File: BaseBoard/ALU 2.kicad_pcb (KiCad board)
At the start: 2 copper layers, 26 parts, among them J1 CONN_01X04, J2 CONN_01X04, J3 CONN_01X03, J4 CONN_01X08, J5 CONN_01X01, J6 CONN_01X04, J7 USB_OTG, U1 74LS138, U10 74LS244, U11 74LS08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

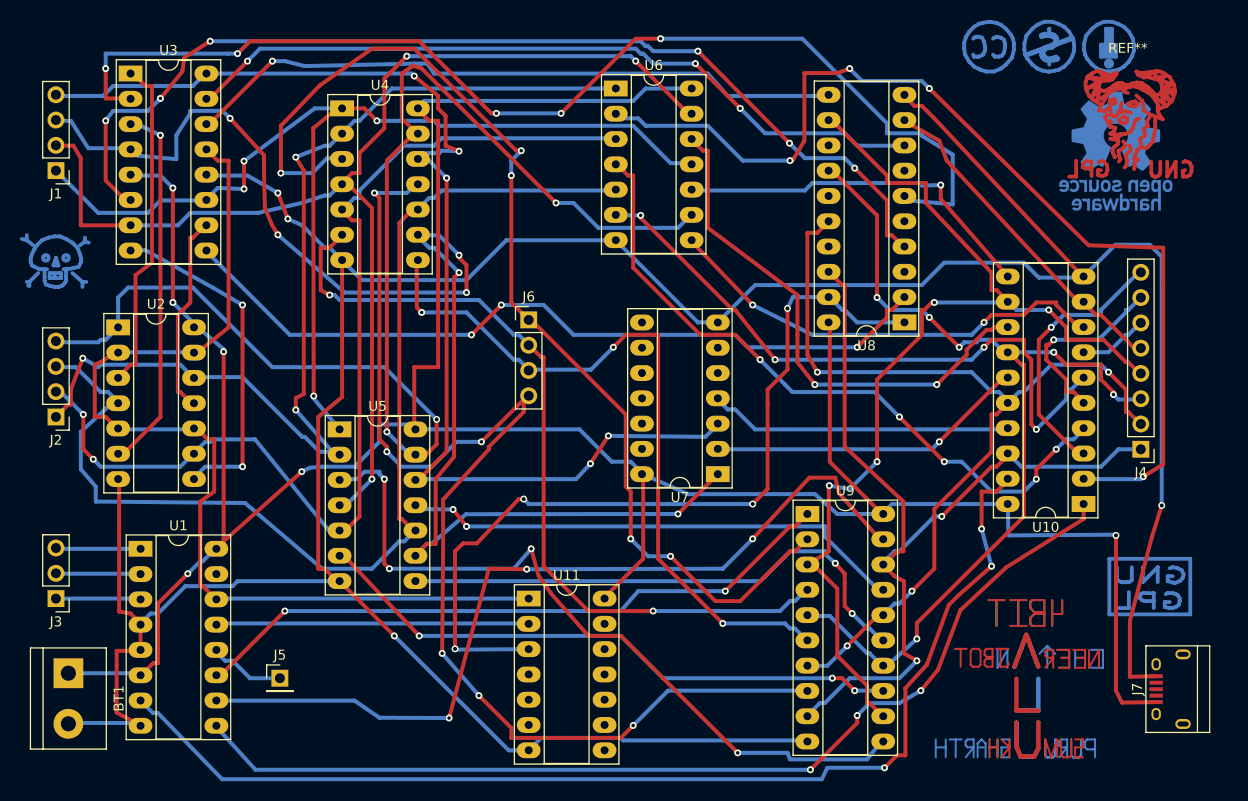
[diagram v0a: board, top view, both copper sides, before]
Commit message: Fixed Fab Issues Pointed out by Neeraj
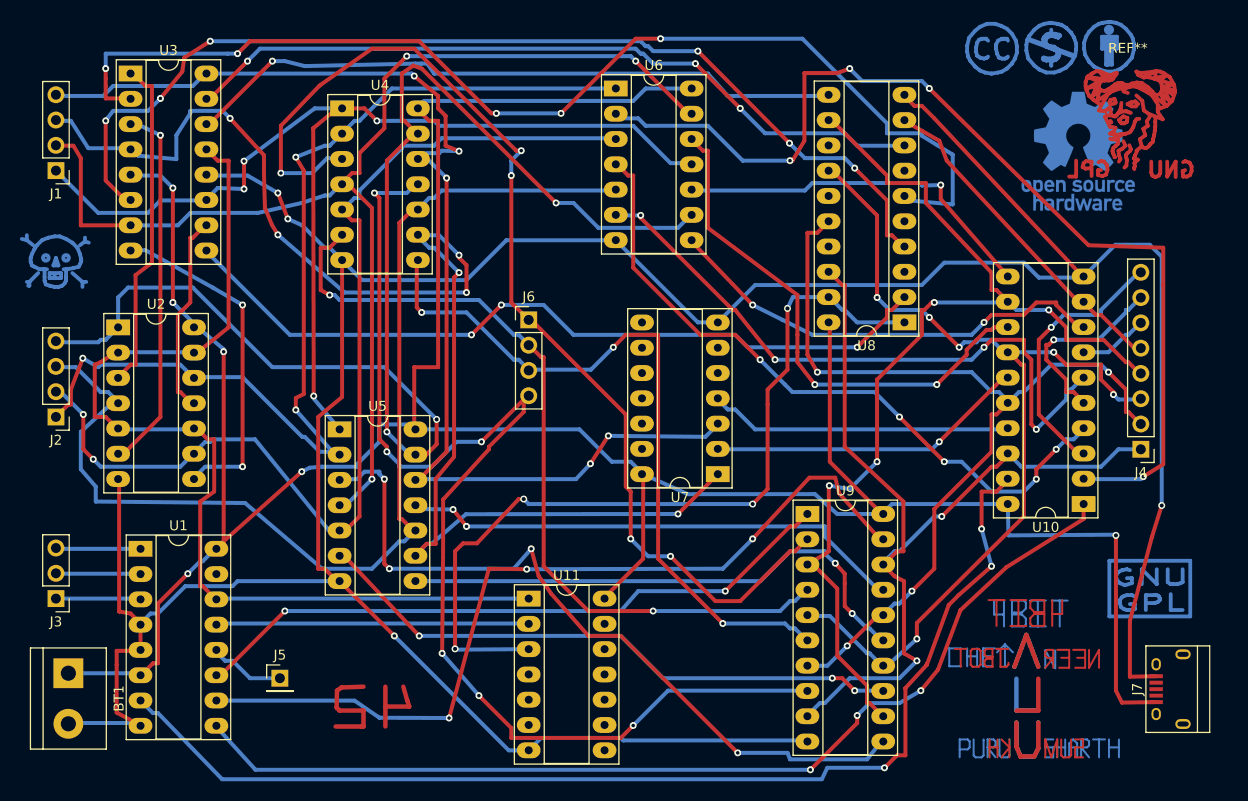
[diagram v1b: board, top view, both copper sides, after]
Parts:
- moved REF** 3.81 mm to (133.2, 72.0)
- moved REF*** 3.80 mm to (122.2, 27.8)
- moved REF** 1.90 mm to (121.2, 17.4), turned to 180 degrees
- turned REF** to 0 degrees
- turned REF** to 180 degrees
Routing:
- net (no net): track 232.7 -> 244.3 mm
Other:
- net class Default: trace_width 0.2 -> 0.45

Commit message: Final Design
Final design of both base and shield board which is ready to roll.
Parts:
- removed the REF** at (127.2, 23.5)
- added REF**: Symbol_GNU-Logo_CopperTop, Symbols:Symbol_GNU-Logo_CopperTop, F.Cu at (125.0, 23.4)
- moved REF*** 5.80 mm to (128.0, 28.0)
- moved REF** 5.06 mm to (128.2, 71.2)
- moved J5 3.72 mm to (39.6, 77.9)
- moved REF** 2.40 mm to (127.0, 19.0)
- moved REF** 2.00 mm to (120.0, 19.0), turned to 0 degrees
- moved J7 1.81 mm to (133.2, 81.8)
- moved REF** 1.71 mm to (113.2, 19.1), turned to 180 degrees
- moved REF** 0.75 mm to (20.2, 39.0)
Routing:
- net Net-(J4-Pad3): track 96.6 -> 139.8 mm, vias 6 -> 4
- net /A2B2: track 331.4 -> 370.3 mm, vias 4 -> 6
- net Net-(J2-Pad3): track 112.0 -> 145.1 mm, vias 0 -> 4
- net Net-(J1-Pad2): track 120.5 -> 145.9 mm, vias 3 -> 6
- net Net-(J4-Pad1): track 91.6 -> 116.0 mm, vias 2 -> 4
- net Net-(J4-Pad4): track 106.3 -> 128.1 mm, vias 4 -> 8
- net Net-(J2-Pad2): track 105.6 -> 125.3 mm, vias 2 -> 4
- net Net-(J4-Pad8): track 27.1 -> 45.9 mm, vias 1 -> 2
- net Net-(BT1-Pad1): track 293.6 -> 312.4 mm, vias 6 -> 16
- net Net-(J7-Pad6): track 0.00 -> 18.2 mm
- net Net-(J2-Pad1): track 104.5 -> 122.5 mm, vias 3 -> 4
- net Net-(U5-Pad6): track 60.4 -> 76.4 mm, vias 3 -> 2
- net Net-(J4-Pad2): track 94.0 -> 110.0 mm, vias 4 -> 6
- net Net-(U1-Pad14): track 102.4 -> 116.1 mm, vias 0 -> 4
- net (no net): track 244.3 -> 256.2 mm
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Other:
- net class Default: trace_width 0.45 -> 0.4
